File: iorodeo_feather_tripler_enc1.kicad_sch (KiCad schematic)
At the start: 10 parts, among them J1 Barrel_Jack_Switch, J2 Conn_01x04, J3 Conn_01x04, J4 Conn_01x04, J5 Conn_01x04, J6 Conn_01x04, SW1 SW_Push_DPDT, U1 feather_wing, U2 feather_wing, U3 feather_wing

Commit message: Fixed issues with JST PH header orientation.
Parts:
- J2, J3, J4: footprint Connector_JST:JST_PH_B4B-PH-SM4-TB_1x04-1MP_P2.00mm_Vertical -> JST_PH_4Pin_Vertical:JST_PH_B4B-PH-SM4-TB_1x04-1MP_P2.00mm_Vertical
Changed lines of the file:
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@@
       (effects (font (size 1.27 1.27)) (justify left))
     )
-    (property "Footprint" "Connector_JST:JST_PH_B4B-PH-SM4-TB_1x04-1MP_P2.00mm_Vertical" (at 200.025 88.9 0)
+    (property "Footprint" "JST_PH_4Pin_Vertical:JST_PH_B4B-PH-SM4-TB_1x04-1MP_P2.00mm_Vertical" (at 200.025 88.9 0)
       (effects (font (size 1.27 1.27)) hide)
     )
@@
       (effects (font (size 1.27 1.27)) (justify left))
     )
-    (property "Footprint" "Connector_JST:JST_PH_B4B-PH-SM4-TB_1x04-1MP_P2.00mm_Vertical" (at 243.205 88.9 0)
+    (property "Footprint" "JST_PH_4Pin_Vertical:JST_PH_B4B-PH-SM4-TB_1x04-1MP_P2.00mm_Vertical" (at 243.205 88.9 0)
       (effects (font (size 1.27 1.27)) hide)
     )
@@
       (effects (font (size 1.27 1.27)) (justify left))
     )
-    (property "Footprint" "Connector_JST:JST_PH_B4B-PH-SM4-TB_1x04-1MP_P2.00mm_Vertical" (at 156.845 88.9 0)
-      (effects (font (size 1.27 1.27)) hide)
-    )
+    (property "Footprint" "JST_PH_4Pin_Vertical:JST_PH_B4B-PH-SM4-TB_1x04-1MP_P2.00mm_Vertical" (at 156.845 88.9 0)
+      (effects (font (size 1.27 1.27)) hide)
+    )

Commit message: Worked on revision 2.
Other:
- note added: "Add jumper pads to digital pins on J2 an J3"
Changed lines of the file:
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@@
     (effects (font (size 2.032 2.032)) (justify left bottom))
+  )
+  (text "Add jumper pads to digital pins on J2 an J3" (at 142.748 149.479 0)
+    (effects (font (size 2.54 2.54) (thickness 1.27) bold) (justify left bottom))
   )
   (text "Grove headers w/ analog inputs and ditigal in/out and serial"

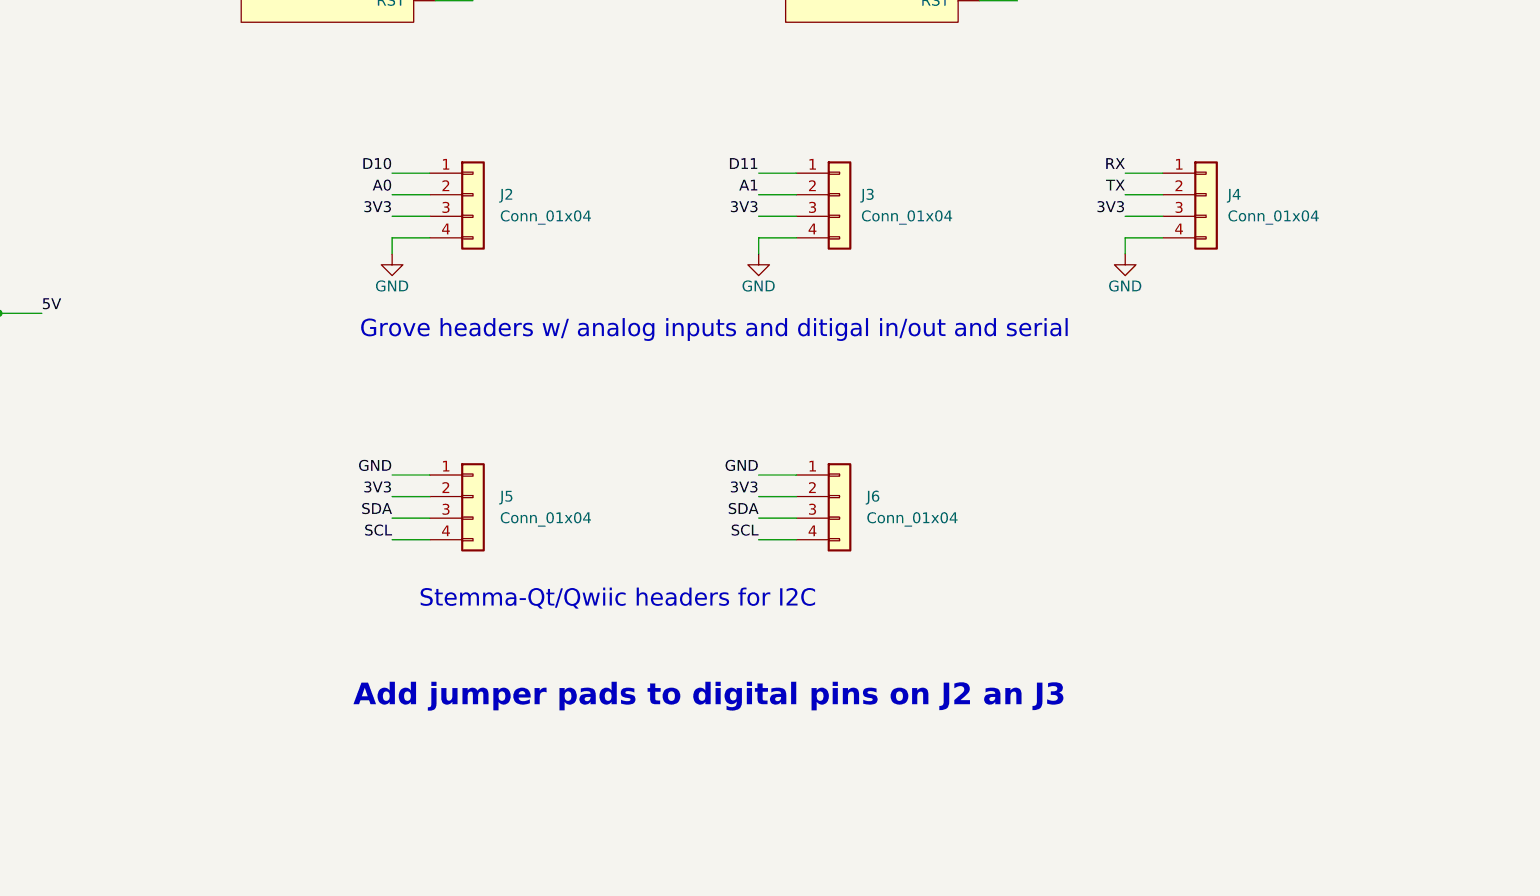
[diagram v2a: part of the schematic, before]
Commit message: More work on revision 2. Added jumper pads to grove headers.
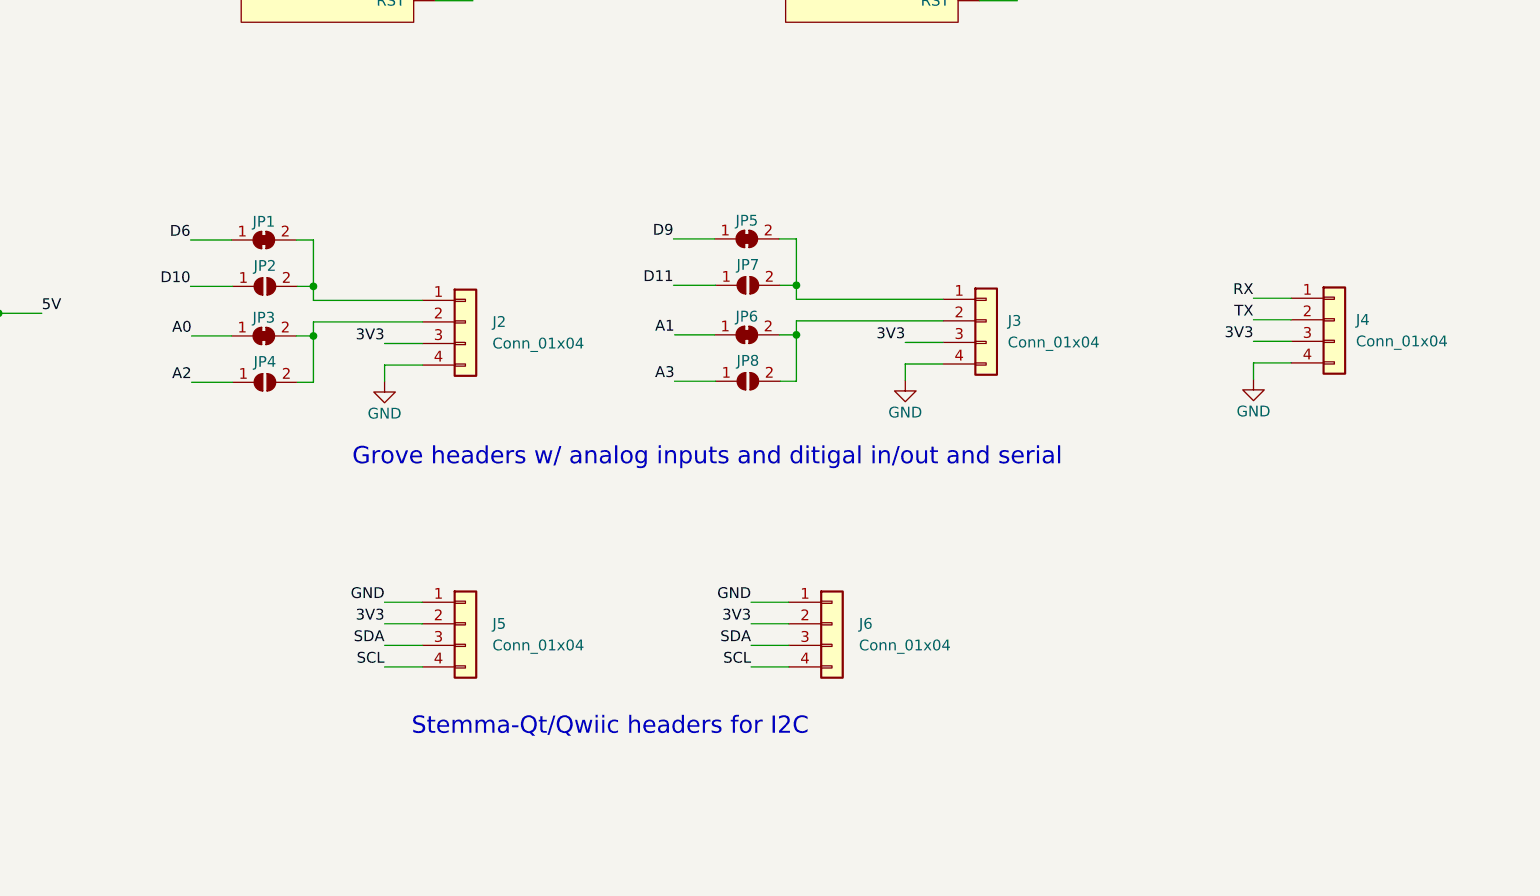
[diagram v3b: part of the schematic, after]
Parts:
- added JP1, JP3, JP5, JP6: SolderJumper_2_Bridged, symbol Jumper:SolderJumper_2_Bridged
- added JP2, JP4, JP7, JP8: SolderJumper_2_Open, symbol Jumper:SolderJumper_2_Open
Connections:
- net A0: now also JP3.1 (A); no longer J2.2 (Pin_2)
- net A1: now also JP6.1 (A); no longer J3.2 (Pin_2)
- net A2: now also JP4.1 (A)
- net A3: now also JP8.1 (A)
- net D10: now also JP2.1 (A); no longer J2.1 (Pin_1)
- net D11: now also JP7.1 (A); no longer J3.1 (Pin_1)
- net D6: now also JP1.1 (A)
- net D9: now also JP5.1 (A)
- new net: J3.1 (Pin_1), JP5.2 (B), JP7.2 (B)
- new net: J3.2 (Pin_2), JP6.2 (B), JP8.2 (B)
- new net: J2.2 (Pin_2), JP3.2 (B), JP4.2 (B)
- new net: J2.1 (Pin_1), JP1.2 (B), JP2.2 (B)
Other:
- note removed: "Add jumper pads to digital pins on J2 an J3"
- moved on the sheet: J2, J3, J4, J5, J6

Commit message: Assigned footprints for jumper pads.
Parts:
- JP1, JP3, JP5: footprint (none) -> Jumper:SolderJumper-2_P1.3mm_Bridged_RoundedPad1.0x1.5mm
- JP2, JP4, JP8: footprint (none) -> Jumper:SolderJumper-2_P1.3mm_Open_RoundedPad1.0x1.5mm
- JP6: renamed from JP7; footprint (none) -> Jumper:SolderJumper-2_P1.3mm_Open_RoundedPad1.0x1.5mm
- JP7: renamed from JP6; footprint (none) -> Jumper:SolderJumper-2_P1.3mm_Bridged_RoundedPad1.0x1.5mm
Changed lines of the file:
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@@
   (symbol (lib_id "Jumper:SolderJumper_2_Open") (at 189.23 99.568 0) (unit 1)
     (in_bom yes) (on_board yes) (dnp no)
-    (property "Reference" "JP7" (at 189.23 97.155 0)
+    (property "Reference" "JP6" (at 189.23 97.155 0)
       (effects (font (size 1.27 1.27)))
     )
@@
       (effects (font (size 1.27 1.27)) hide)
     )
-    (property "Footprint" "" (at 189.23 99.568 0)
+    (property "Footprint" "Jumper:SolderJumper-2_P1.3mm_Open_RoundedPad1.0x1.5mm" (at 189.23 99.568 0)
       (effects (font (size 1.27 1.27)) hide)
     )
@@
       (project "iorodeo_feather_tripler_enc1"
         (path "/69dbd3c8-f5a8-4540-8250-0a9adfd5597d"
-          (reference "JP7") (unit 1)
+          (reference "JP6") (unit 1)
         )
       )
@@
       (effects (font (size 1.27 1.27)) hide)
     )
-    (property "Footprint" "" (at 189.23 110.871 0)
+    (property "Footprint" "Jumper:SolderJumper-2_P1.3mm_Open_RoundedPad1.0x1.5mm" (at 189.23 110.871 0)
       (effects (font (size 1.27 1.27)) hide)
     )
@@
       (effects (font (size 1.27 1.27)) hide)
     )
-    (property "Footprint" "" (at 189.103 94.107 0)
+    (property "Footprint" "Jumper:SolderJumper-2_P1.3mm_Bridged_RoundedPad1.0x1.5mm" (at 189.103 94.107 0)
       (effects (font (size 1.27 1.27)) hide)
     )
@@
       (effects (font (size 1.27 1.27)) hide)
     )
-    (property "Footprint" "" (at 132.207 105.537 0)
+    (property "Footprint" "Jumper:SolderJumper-2_P1.3mm_Bridged_RoundedPad1.0x1.5mm" (at 132.207 105.537 0)
       (effects (font (size 1.27 1.27)) hide)
     )
@@
   (symbol (lib_id "Jumper:SolderJumper_2_Bridged") (at 189.103 105.41 0) (unit 1)
     (in_bom yes) (on_board yes) (dnp no)
-    (property "Reference" "JP6" (at 189.103 103.251 0)
+    (property "Reference" "JP7" (at 189.103 103.251 0)
       (effects (font (size 1.27 1.27)))
     )
@@
       (effects (font (size 1.27 1.27)) hide)
     )
-    (property "Footprint" "" (at 189.103 105.41 0)
+    (property "Footprint" "Jumper:SolderJumper-2_P1.3mm_Bridged_RoundedPad1.0x1.5mm" (at 189.103 105.41 0)
       (effects (font (size 1.27 1.27)) hide)
     )
@@
       (project "iorodeo_feather_tripler_enc1"
         (path "/69dbd3c8-f5a8-4540-8250-0a9adfd5597d"
-          (reference "JP6") (unit 1)
+          (reference "JP7") (unit 1)
         )
       )
@@
       (effects (font (size 1.27 1.27)) hide)
     )
-    (property "Footprint" "" (at 132.334 99.695 0)
+    (property "Footprint" "Jumper:SolderJumper-2_P1.3mm_Open_RoundedPad1.0x1.5mm" (at 132.334 99.695 0)
       (effects (font (size 1.27 1.27)) hide)
     )
@@
       (effects (font (size 1.27 1.27)) hide)
     )
-    (property "Footprint" "" (at 132.334 110.998 0)
+    (property "Footprint" "Jumper:SolderJumper-2_P1.3mm_Open_RoundedPad1.0x1.5mm" (at 132.334 110.998 0)
       (effects (font (size 1.27 1.27)) hide)
     )
@@
       (effects (font (size 1.27 1.27)) hide)
     )
-    (property "Footprint" "" (at 132.207 94.234 0)
-      (effects (font (size 1.27 1.27)) hide)
-    )
+    (property "Footprint" "Jumper:SolderJumper-2_P1.3mm_Bridged_RoundedPad1.0x1.5mm" (at 132.207 94.234 0)
+      (effects (font (size 1.27 1.27)) hide)
+    )

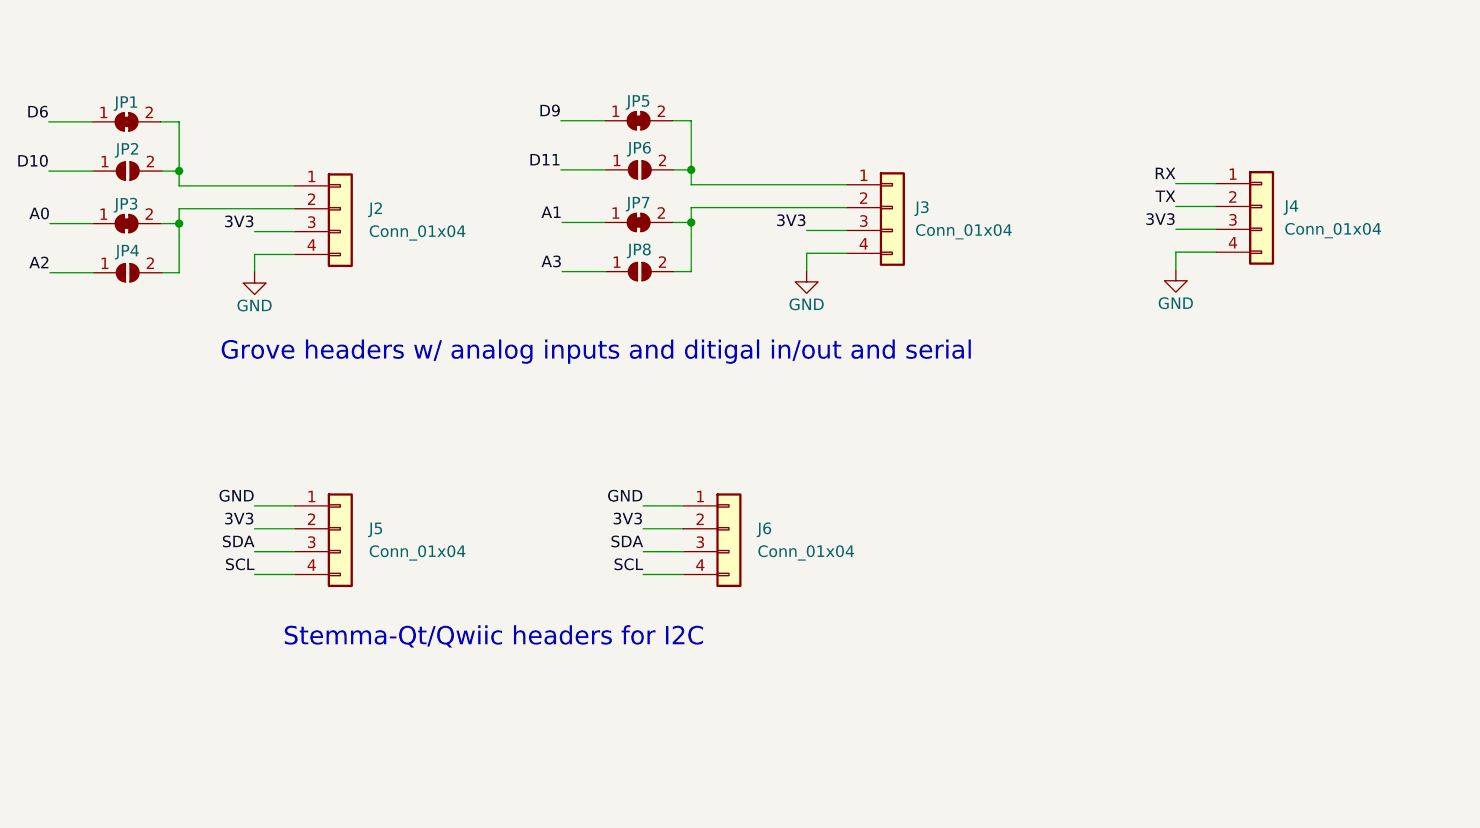
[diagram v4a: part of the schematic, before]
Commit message: Finished rerouting board.  Remade production files. Need to be checked.
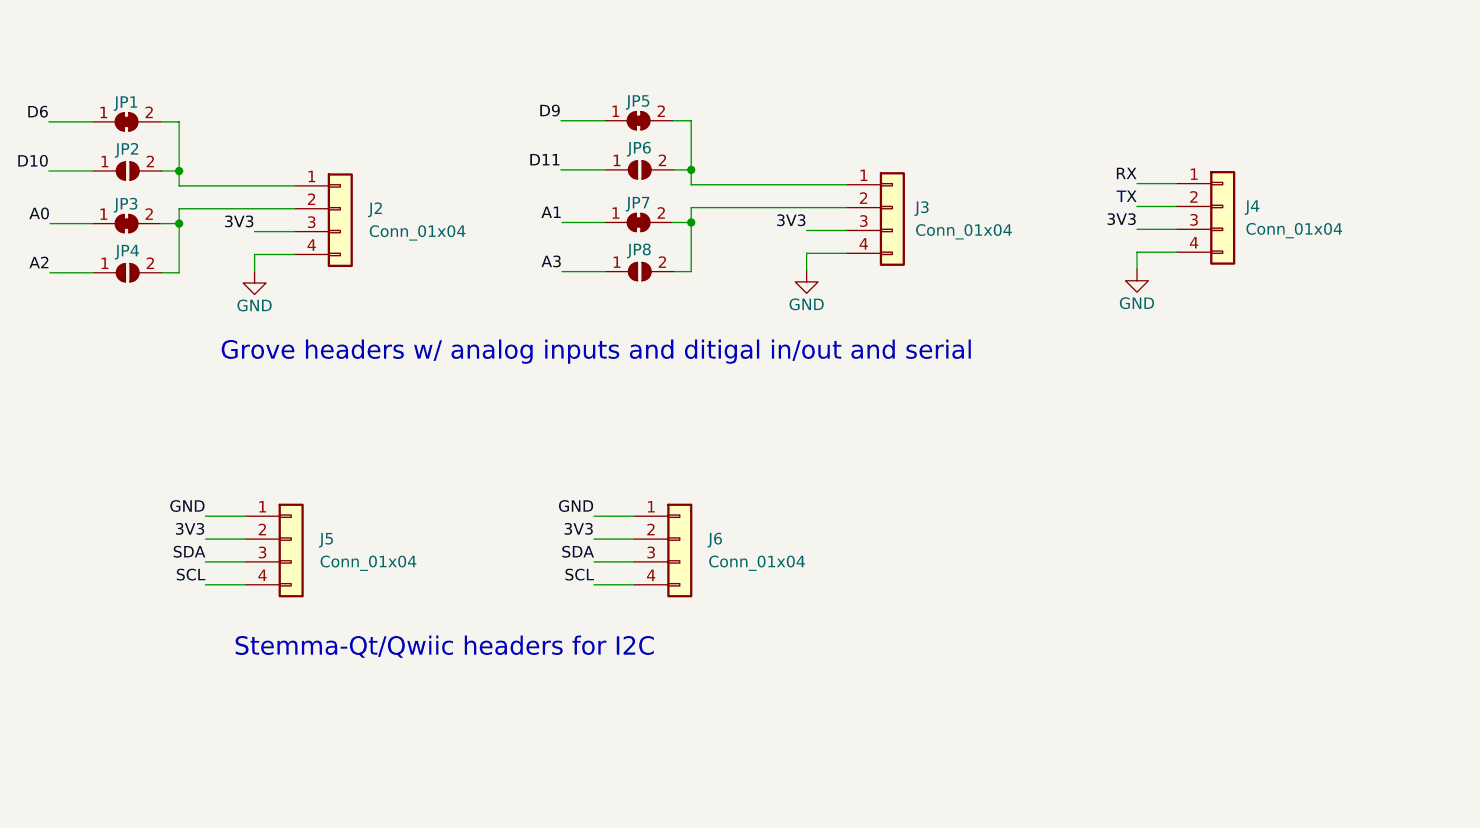
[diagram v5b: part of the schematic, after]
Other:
- moved on the sheet: J4, J5, J6
